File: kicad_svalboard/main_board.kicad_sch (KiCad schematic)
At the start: 35 parts, among them J1 Conn_01x07, J2 Conn_01x07, J3 Conn_01x07, J4 Conn_01x07, J5 Conn_01x07, J6 PJ-320D, J8 Conn_01x07, Q1 Q_NPN_BEC, Q2 Q_NPN_BEC, Q3 Q_NPN_BEC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

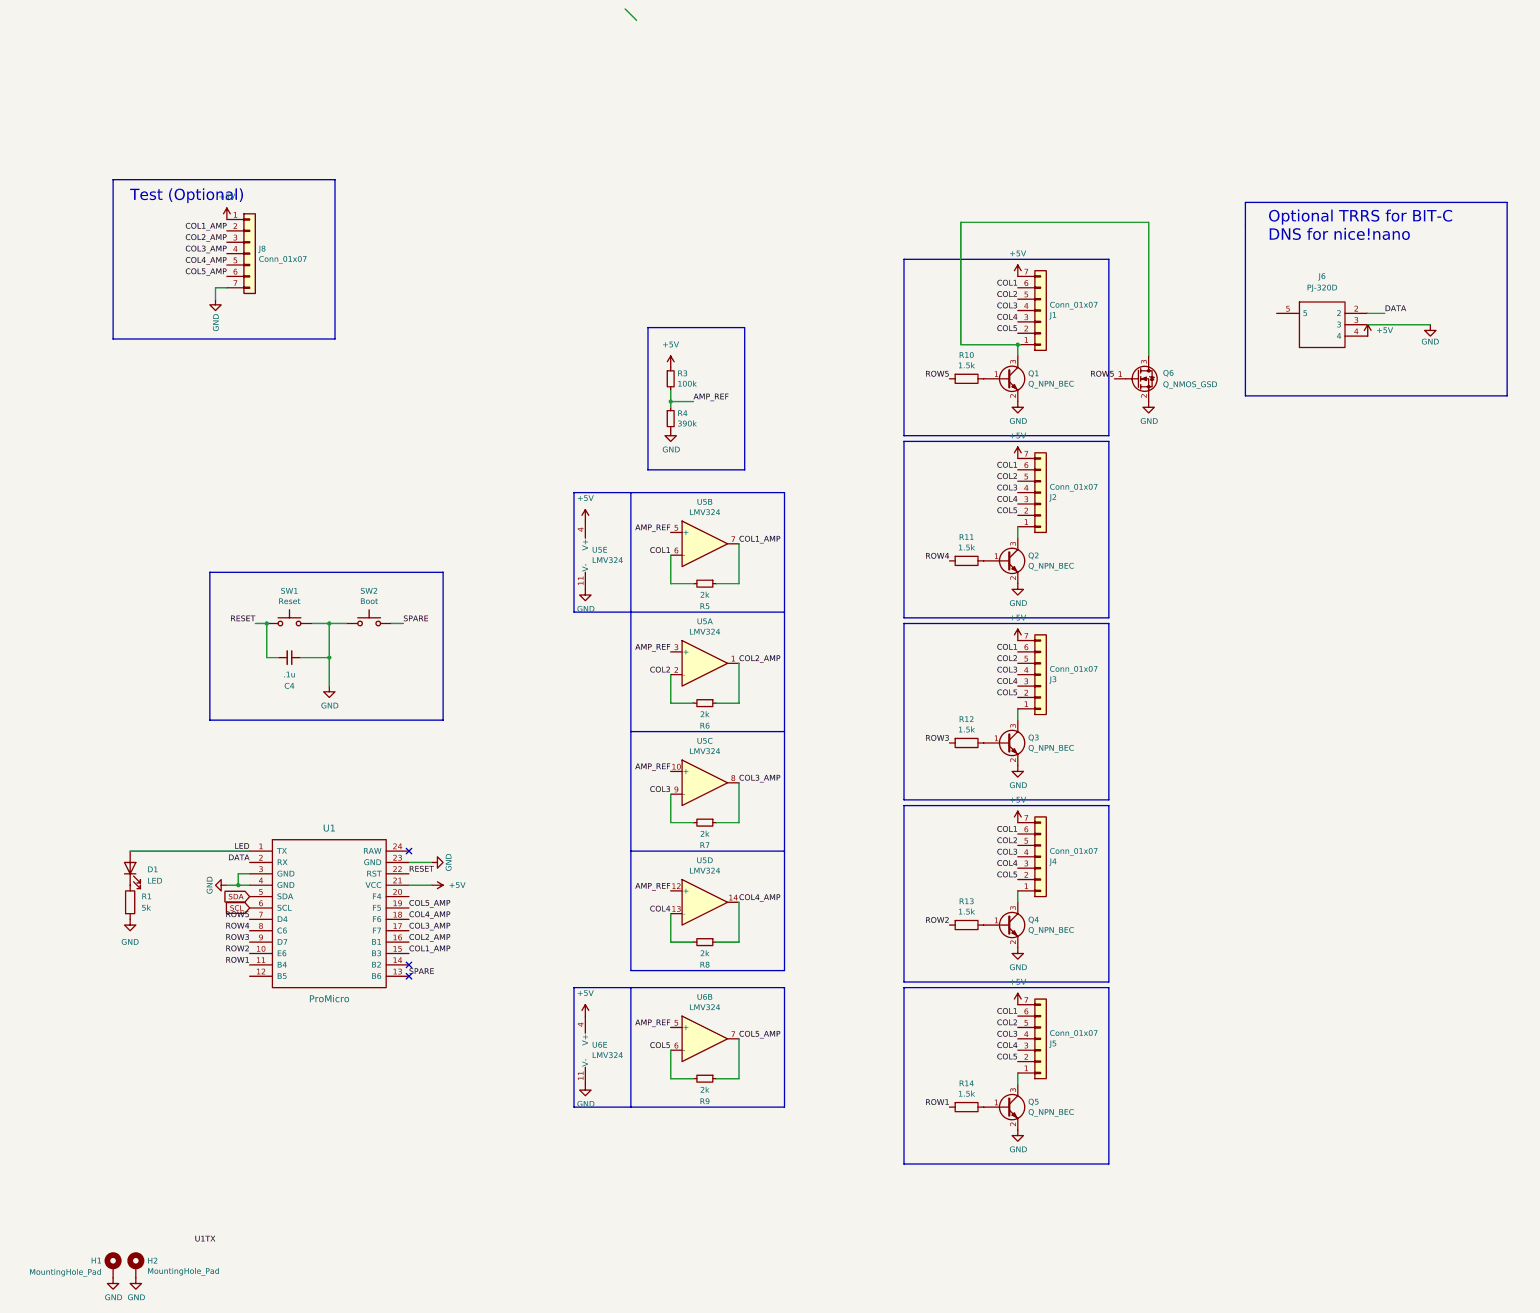
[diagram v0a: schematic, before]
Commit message: Removed datasheets folder, updated design with layouts for cluster and main PCB.  still need FFC connectors on main PCB
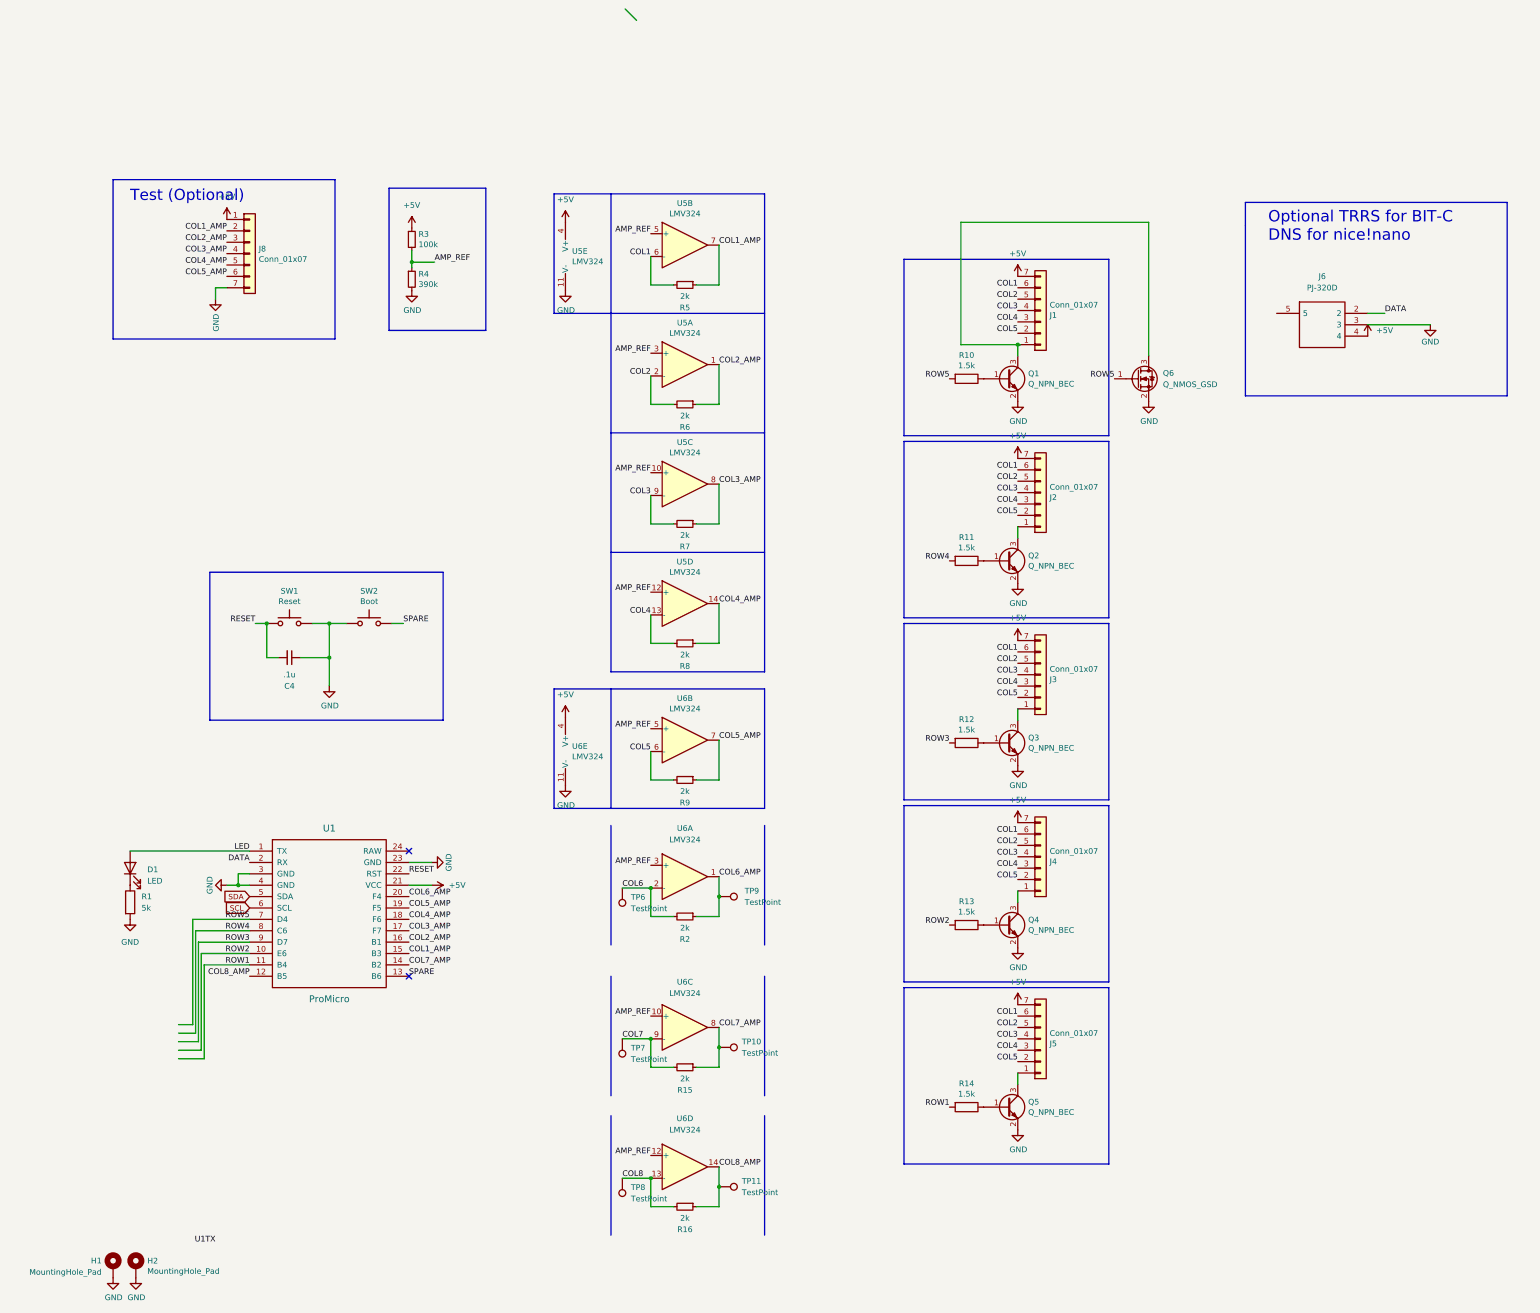
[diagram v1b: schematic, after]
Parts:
- added R15, R16, R2: 2k, Resistor_SMD:R_0805_2012Metric_Pad1.20x1.40mm_HandSolder, symbol Device:R_Small
- added TP10, TP11, TP6, TP7, TP8, TP9: TestPoint, TestPoint:TestPoint_THTPad_D1.0mm_Drill0.5mm, symbol lalboard:TestPoint
- added unit 4 of U6
- added unit 1 of U6
- added unit 3 of U6
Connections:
- net AMP_REF: now also U6.10 (+), U6.12 (+), U6.3 (+)
- net COL8_AMP: now reaches U1.12 (B5)
- net COL8_AMP: now also R16.1, TP11.1, U6.14
- net COL7_AMP: now reaches U1.14 (B2)
- net COL7_AMP: now also R15.1, TP10.1, U6.8
- net COL6_AMP: now reaches U1.20 (F4)
- net COL6_AMP: now also R2.1, TP9.1, U6.1
- new net COL6: R2.2, TP6.1, U6.2 (-)
- new net COL7: R15.2, TP7.1, U6.9 (-)
- new net COL8: R16.2, TP8.1, U6.13 (-)
- no-connect marks 3 -> 2
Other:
- moved on the sheet: R3, R4, R5, R6, R7, R8, R9, U5A, U5B, U5C, U5D, U5E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
